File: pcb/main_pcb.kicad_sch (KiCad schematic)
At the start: 44 parts, among them J1 Conn_01x06_Socket, J2 Conn_01x10_Pin, J4 USB_C_Receptacle_USB2.0, Q1 Si2323DS, SW1 SW_Push, SW2 SW_Push, SW3 SW_Push, U1 ESP32-H2-MINI-1, U2 LM5165Y, Y1 32.768KHz

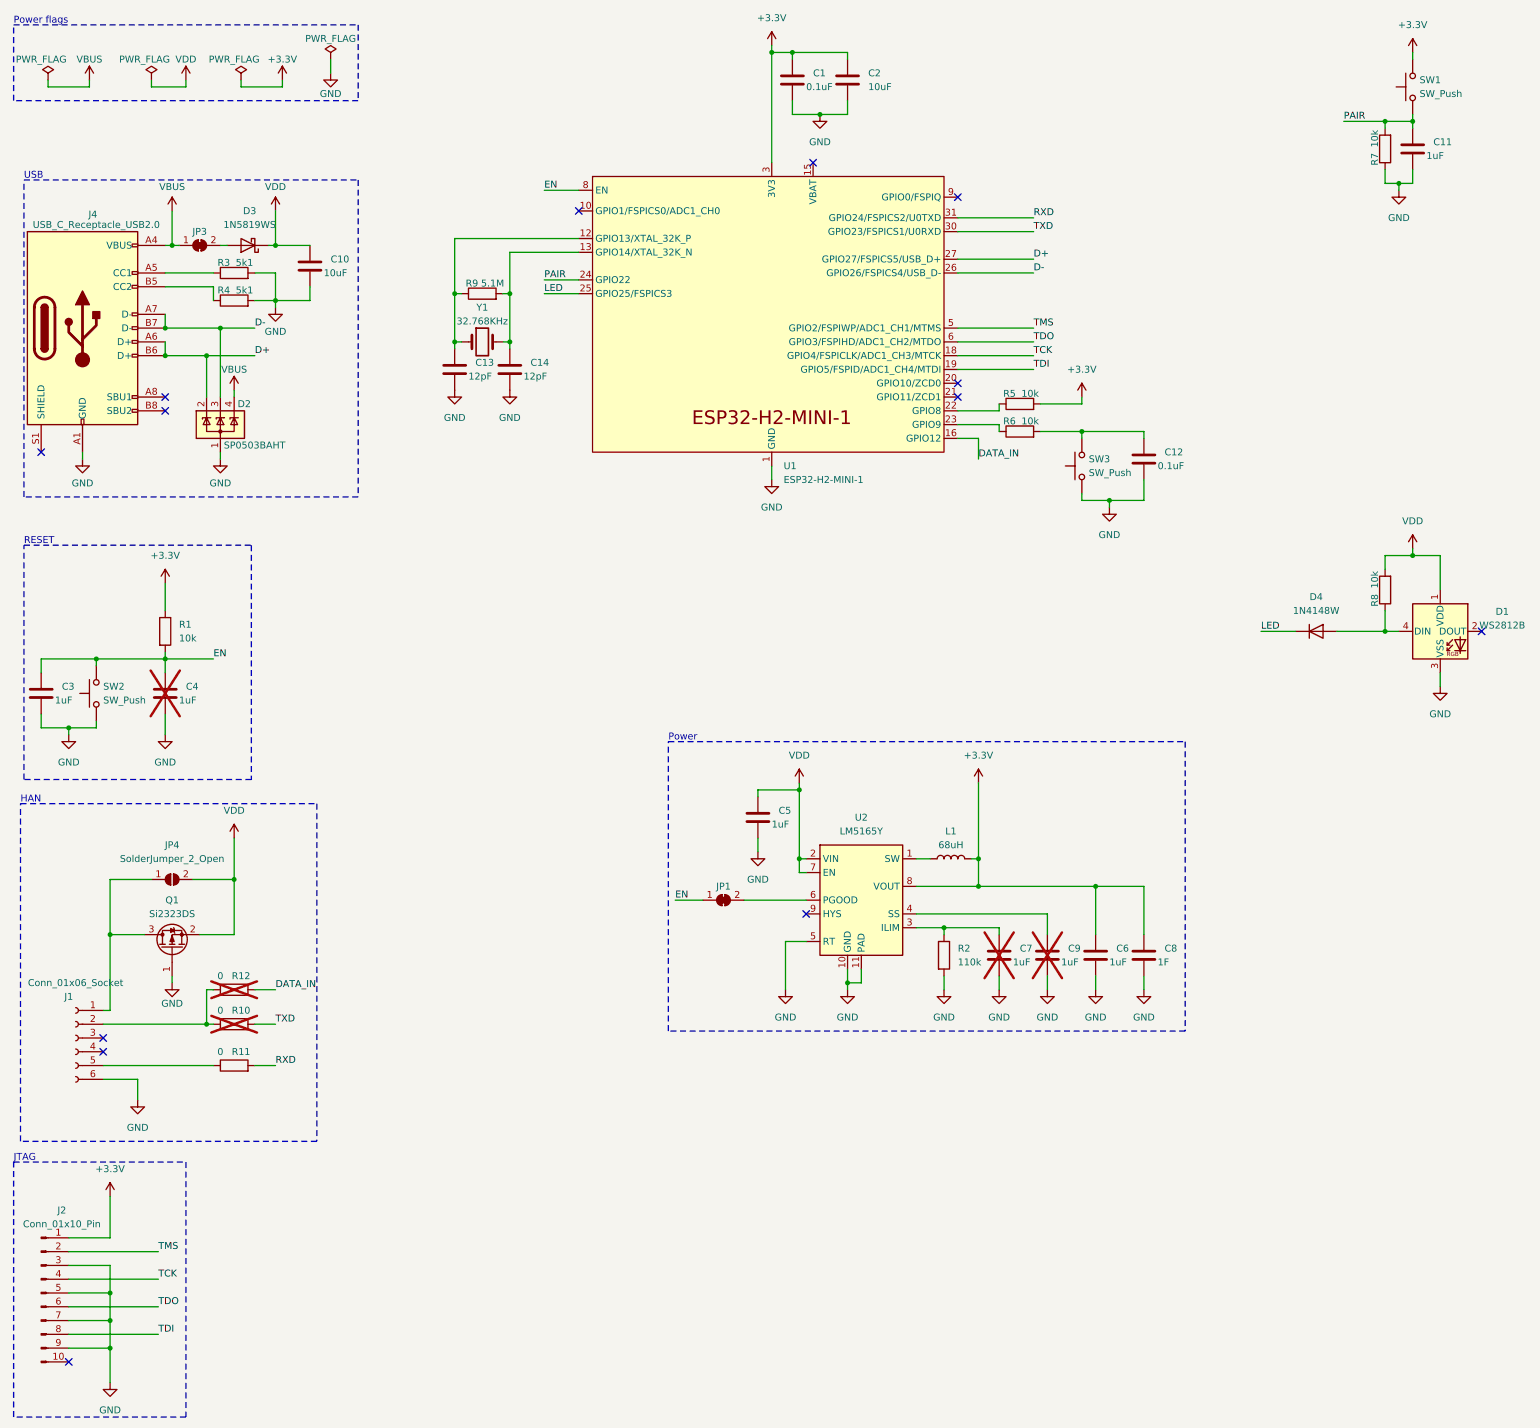
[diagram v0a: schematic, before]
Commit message: Remove JTAG connector
Planning on using the built in JTAG via USB.
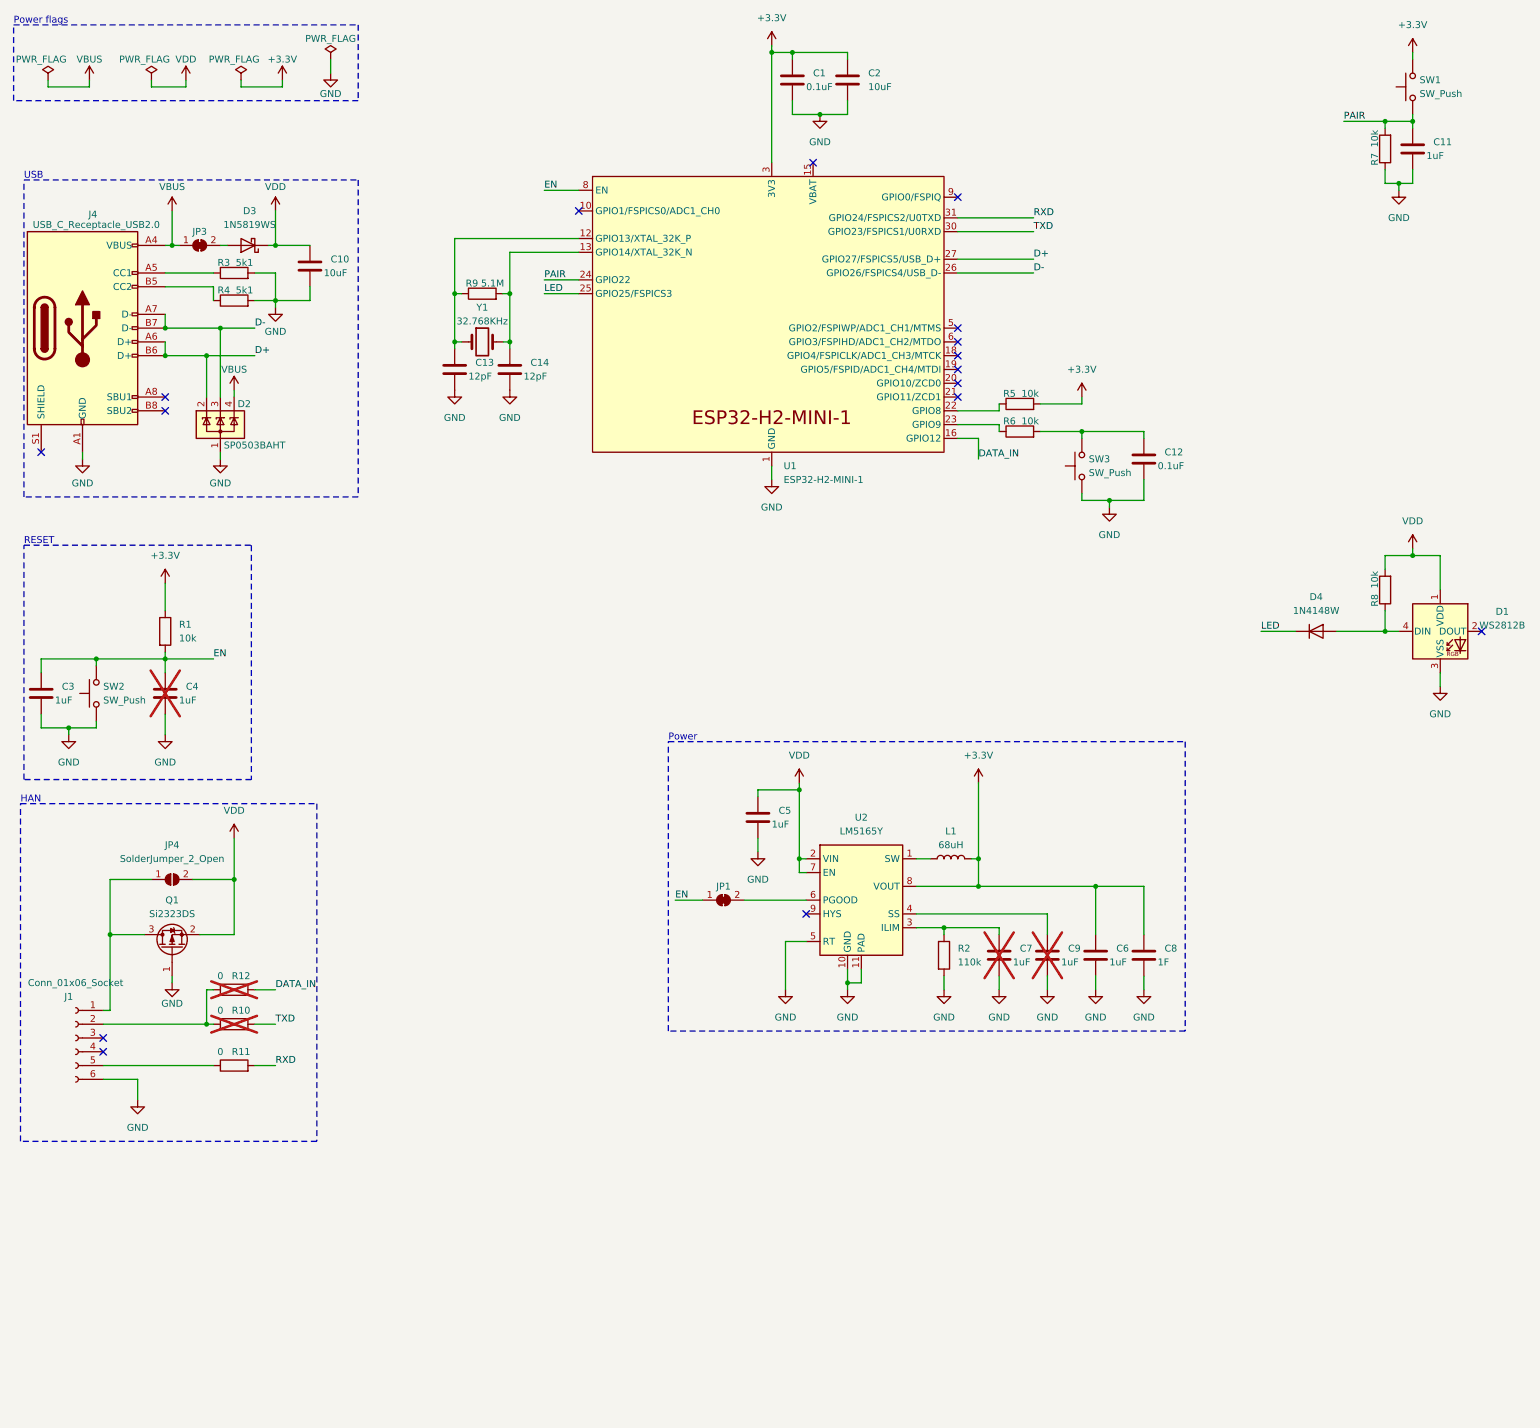
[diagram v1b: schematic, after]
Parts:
- removed J2: Conn_01x10_Pin, Connector:Tag-Connect_TC2050-IDC-FP_2x05_P1.27mm_Vertical, symbol Connector:Conn_01x10_Pin
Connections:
- net TCK: no longer names the net of U1.18 (GPIO4/FSPICLK/ADC1_CH3/MTCK)
- net TDI: no longer names the net of U1.19 (GPIO5/FSPID/ADC1_CH4/MTDI)
- net TDO: no longer names the net of U1.6 (GPIO3/FSPIHD/ADC1_CH2/MTDO)
- net TMS: no longer names the net of U1.5 (GPIO2/FSPIWP/ADC1_CH1/MTMS)
- no-connect marks 13 -> 16
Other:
- note removed: "JTAG"
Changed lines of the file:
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@@
   (junction (at 101.6 72.39) (diameter 0) (color 0 0 0 0)
   )
-  (junction (at 38.1 266.7) (diameter 0) (color 0 0 0 0)
-  )
   (junction (at 165.1 163.83) (diameter 0) (color 0 0 0 0)
   )
@@
   (junction (at 101.6 81.28) (diameter 0) (color 0 0 0 0)
   )
-  (junction (at 38.1 261.62) (diameter 0) (color 0 0 0 0)
-  )
   (junction (at 163.83 27.94) (diameter 0) (color 0 0 0 0)
   )
@@
   )
   (junction (at 219.71 181.61) (diameter 0) (color 0 0 0 0)
-  )
-  (junction (at 38.1 256.54) (diameter 0) (color 0 0 0 0)
   )
   (no_connect (at 25.4 101.6))
   (no_connect (at 36.83 209.55))
+  (no_connect (at 194.31 78.74))
   (no_connect (at 194.31 54.61))
-  (no_connect (at 30.48 269.24))
   (no_connect (at 290.83 134.62))
   (no_connect (at 194.31 91.44))
   (no_connect (at 124.46 57.15))
+  (no_connect (at 194.31 86.36))
   (no_connect (at 36.83 212.09))
+  (no_connect (at 194.31 81.28))
   (no_connect (at 194.31 88.9))
   (no_connect (at 166.37 186.69))
@@
   (no_connect (at 48.26 91.44))
   (no_connect (at 48.26 93.98))
+  (no_connect (at 194.31 83.82))
   (wire (pts (xy 186.69 186.69) (xy 210.82 186.69))
     (stroke (width 0) (type default))
@@
     (stroke (width 0) (type default))
   )
-  (wire (pts (xy 194.31 83.82) (xy 208.28 83.82))
-    (stroke (width 0) (type default))
-  )
   (wire (pts (xy 222.25 110.49) (xy 217.17 110.49))
     (stroke (width 0) (type default))
@@
     (stroke (width 0) (type default))
   )
-  (wire (pts (xy 38.1 261.62) (xy 38.1 266.7))
-    (stroke (width 0) (type default))
-  )
   (wire (pts (xy 48.26 125.73) (xy 48.26 130.81))
     (stroke (width 0) (type default))
@@
     (stroke (width 0) (type default))
   )
-  (wire (pts (xy 30.48 266.7) (xy 38.1 266.7))
-    (stroke (width 0) (type default))
-  )
   (wire (pts (xy 25.4 139.7) (xy 35.56 139.7))
     (stroke (width 0) (type default))
@@
     (stroke (width 0) (type default))
   )
-  (wire (pts (xy 194.31 78.74) (xy 208.28 78.74))
-    (stroke (width 0) (type default))
-  )
   (wire (pts (xy 210.82 198.12) (xy 210.82 200.66))
     (stroke (width 0) (type default))
@@
     (stroke (width 0) (type default))
   )
-  (wire (pts (xy 30.48 261.62) (xy 38.1 261.62))
-    (stroke (width 0) (type default))
-  )
-  (wire (pts (xy 38.1 251.46) (xy 38.1 256.54))
-    (stroke (width 0) (type default))
-  )
   (wire (pts (xy 173.99 27.94) (xy 163.83 27.94))
     (stroke (width 0) (type default))
@@
     (stroke (width 0) (type default))
   )
-  (wire (pts (xy 30.48 259.08) (xy 46.99 259.08))
-    (stroke (width 0) (type default))
-  )
   (wire (pts (xy 194.31 66.04) (xy 208.28 66.04))
     (stroke (width 0) (type default))
@@
     (stroke (width 0) (type default))
   )
-  (wire (pts (xy 30.48 256.54) (xy 38.1 256.54))
-    (stroke (width 0) (type default))
-  )
   (wire (pts (xy 228.6 99.06) (xy 228.6 97.79))
     (stroke (width 0) (type default))
@@
     (stroke (width 0) (type default))
   )
-  (wire (pts (xy 30.48 251.46) (xy 38.1 251.46))
-    (stroke (width 0) (type default))
-  )
   (wire (pts (xy 166.37 176.53) (xy 165.1 176.53))
     (stroke (width 0) (type default))
@@
     (stroke (width 0) (type default))
   )
-  (wire (pts (xy 194.31 86.36) (xy 208.28 86.36))
-    (stroke (width 0) (type default))
-  )
   (wire (pts (xy 48.26 139.7) (xy 48.26 142.24))
     (stroke (width 0) (type default))
@@
     (stroke (width 0) (type default))
   )
-  (wire (pts (xy 194.31 81.28) (xy 208.28 81.28))
-    (stroke (width 0) (type default))
-  )
   (wire (pts (xy 278.13 120.65) (xy 283.21 120.65))
     (stroke (width 0) (type default))
@@
     (stroke (width 0) (type default))
   )
-  (wire (pts (xy 38.1 246.38) (xy 38.1 238.76))
-    (stroke (width 0) (type default))
-  )
   (wire (pts (xy 26.67 34.29) (xy 34.29 34.29))
     (stroke (width 0) (type default))
@@
     (stroke (width 0) (type default))
   )
-  (wire (pts (xy 38.1 266.7) (xy 38.1 273.05))
-    (stroke (width 0) (type default))
-  )
-  (wire (pts (xy 30.48 248.92) (xy 46.99 248.92))
-    (stroke (width 0) (type default))
-  )
   (wire (pts (xy 198.12 181.61) (xy 198.12 176.53))
     (stroke (width 0) (type default))
@@
     (stroke (width 0) (type default))
   )
-  (wire (pts (xy 30.48 246.38) (xy 38.1 246.38))
-    (stroke (width 0) (type default))
-  )
   (wire (pts (xy 36.83 214.63) (xy 57.15 214.63))
     (stroke (width 0) (type default))
@@
     (stroke (width 0) (type default))
   )
-  (wire (pts (xy 30.48 254) (xy 46.99 254))
-    (stroke (width 0) (type default))
-  )
-  (wire (pts (xy 38.1 256.54) (xy 38.1 261.62))
-    (stroke (width 0) (type default))
-  )
   (wire (pts (xy 48.26 68.58) (xy 57.15 68.58))
     (stroke (width 0) (type default))
@@
   )
   (wire (pts (xy 163.83 36.83) (xy 163.83 39.37))
-    (stroke (width 0) (type default))
-  )
-  (wire (pts (xy 30.48 264.16) (xy 46.99 264.16))
     (stroke (width 0) (type default))
   )
@@
     (fill (type none))
   )
-  (rectangle (start 20.32 232.41) (end 52.07 279.4)
-    (stroke (width 0) (type dash))
-    (fill (type none))
-  )
   (rectangle (start 22.225 118.745) (end 64.135 161.925)
     (stroke (width 0) (type dash))
@@
     (effects (font (size 1.27 1.27)) (justify left bottom))
   )
-  (text "JTAG\n" (at 20.32 232.41 0)
-    (effects (font (size 1.27 1.27)) (justify left bottom))
-  )
   (text "Power\n" (at 140.97 154.94 0)
     (effects (font (size 1.27 1.27)) (justify left bottom))
@@
     (effects (font (size 1.27 1.27)) (justify left bottom))
   )
-  (label "TMS" (at 46.99 248.92 0) (fields_autoplaced)
-    (effects (font (size 1.27 1.27)) (justify left bottom))
-  )
-  (label "TCK" (at 208.28 83.82 0) (fields_autoplaced)
-    (effects (font (size 1.27 1.27)) (justify left bottom))
-  )
   (label "DATA_IN" (at 68.58 200.66 0) (fields_autoplaced)
     (effects (font (size 1.27 1.27)) (justify left bottom))
@@
     (effects (font (size 1.27 1.27)) (justify left bottom))
   )
-  (label "TDO" (at 46.99 259.08 0) (fields_autoplaced)
-    (effects (font (size 1.27 1.27)) (justify left bottom))
-  )
-  (label "TMS" (at 208.28 78.74 0) (fields_autoplaced)
-    (effects (font (size 1.27 1.27)) (justify left bottom))
-  )
-  (label "TDO" (at 208.28 81.28 0) (fields_autoplaced)
-    (effects (font (size 1.27 1.27)) (justify left bottom))
-  )
-  (label "TCK" (at 46.99 254 0) (fields_autoplaced)
-    (effects (font (size 1.27 1.27)) (justify left bottom))
-  )
   (label "EN" (at 142.24 184.15 0) (fields_autoplaced)
     (effects (font (size 1.27 1.27)) (justify left bottom))
@@
     (effects (font (size 1.27 1.27)) (justify left bottom))
   )
-  (label "TDI" (at 208.28 86.36 0) (fields_autoplaced)
-    (effects (font (size 1.27 1.27)) (justify left bottom))
-  )
   (label "EN" (at 57.15 139.7 0) (fields_autoplaced)
     (effects (font (size 1.27 1.27)) (justify left bottom))
@@
   )
   (label "D+" (at 208.28 66.04 0) (fields_autoplaced)
-    (effects (font (size 1.27 1.27)) (justify left bottom))
-  )
-  (label "TDI" (at 46.99 264.16 0) (fields_autoplaced)
     (effects (font (size 1.27 1.27)) (justify left bottom))
   )
@@
     )
   )
-  (symbol (lib_id "Connector:Conn_01x10_Pin") (at 25.4 256.54 0) (unit 1)
-    (in_bom yes) (on_board yes) (dnp no)
-    (property "Reference" "J2" (at 29.21 241.3 0)
-      (effects (font (size 1.27 1.27)))
-    )
-    (property "Value" "Conn_01x10_Pin" (at 29.21 243.84 0)
-      (effects (font (size 1.27 1.27)))
-    )
-    (property "Footprint" "Connector:Tag-Connect_TC2050-IDC-FP_2x05_P1.27mm_Vertical" (at 25.4 256.54 0)
-      (effects (font (size 1.27 1.27)) hide)
-    )
-    (property "Datasheet" "~" (at 25.4 256.54 0)
-      (effects (font (size 1.27 1.27)) hide)
-    )
-    (pin "3")
-    (pin "8")
-    (pin "9")
-    (pin "6")
-    (pin "2")
-    (pin "4")
-    (pin "1")
-    (pin "5")
-    (pin "10")
-    (pin "7")
-    (instances
-      (project "main_pcb"
-        (path "/6204b7c2-8814-41ee-9243-5078f55f08d4"
-          (reference "J2") (unit 1)
-        )
-      )
-    )
-  )
   (symbol (lib_id "power:GND") (at 168.91 39.37 0) (unit 1)
     (in_bom yes) (on_board yes) (dnp no) (fields_autoplaced)
@@
         (path "/6204b7c2-8814-41ee-9243-5078f55f08d4"
           (reference "#PWR029") (unit 1)
-        )
-      )
-    )
-  )
-  (symbol (lib_id "power:+3.3V") (at 38.1 238.76 0) (unit 1)
-    (in_bom yes) (on_board yes) (dnp no) (fields_autoplaced)
-    (property "Reference" "#PWR018" (at 38.1 242.57 0)
-      (effects (font (size 1.27 1.27)) hide)
-    )
-    (property "Value" "+3.3V" (at 38.1 233.68 0)
-      (effects (font (size 1.27 1.27)))
-    )
-    (property "Footprint" "" (at 38.1 238.76 0)
-      (effects (font (size 1.27 1.27)) hide)
-    )
-    (property "Datasheet" "" (at 38.1 238.76 0)
-      (effects (font (size 1.27 1.27)) hide)
-    )
-    (pin "1")
-    (instances
-      (project "main_pcb"
-        (path "/6204b7c2-8814-41ee-9243-5078f55f08d4"
-          (reference "#PWR018") (unit 1)
         )
       )
@@
         )
       )
-    )
-  )
-  (symbol (lib_id "power:GND") (at 38.1 273.05 0) (unit 1)
-    (in_bom yes) (on_board yes) (dnp no) (fields_autoplaced)
-    (property "Reference" "#PWR019" (at 38.1 279.4 0)
-      (effects (font (size 1.27 1.27)) hide)
-    )
-    (property "Value" "GND" (at 38.1 278.13 0)
-      (effects (font (size 1.27 1.27)))
-    )
-    (property "Footprint" "" (at 38.1 273.05 0)
-      (effects (font (size 1.27 1.27)) hide)
-    )
-    (property "Datasheet" "" (at 38.1 273.05 0)
-      (effects (font (size 1.27 1.27)) hide)
-    )
-    (pin "1")
-    (instances
-      (project "main_pcb"
-        (path "/6204b7c2-8814-41ee-9243-5078f55f08d4"
-          (reference "#PWR019") (unit 1)
-        )
-      )
